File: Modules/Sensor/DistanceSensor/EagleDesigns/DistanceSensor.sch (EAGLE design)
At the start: 10 parts, among them U1 TINY85-20-DIP

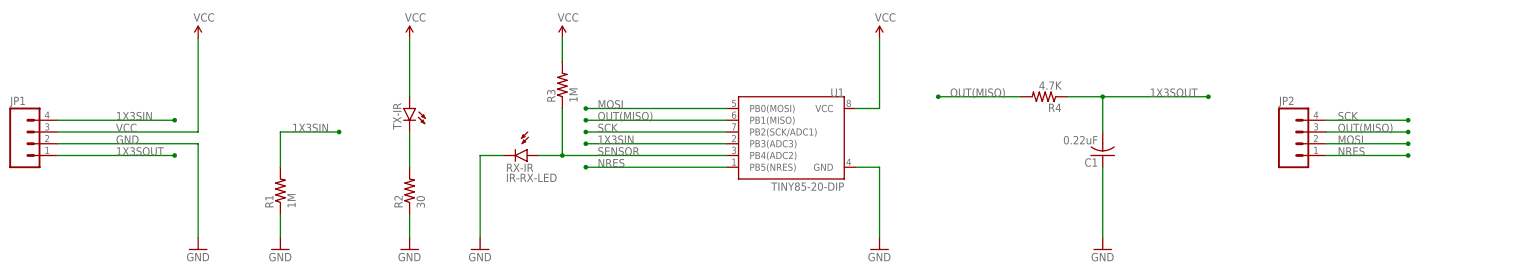
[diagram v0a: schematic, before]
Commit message: DistanceSensor: added another IR-TX LED #9
to increase the range of the module.
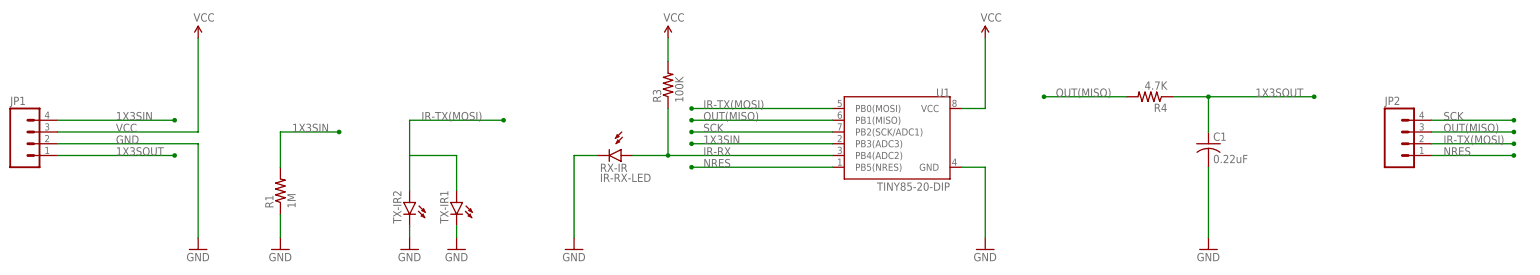
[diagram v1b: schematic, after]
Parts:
- removed R2: 30, adafruit:R-US_R0603
- removed TX-IR: (no value), SparkFun-LED:LED5MM
- added TX-IR1, TX-IR2: (no value), SparkFun-LED:LED5MM
- C1: device adafruit:C-USC0402 -> adafruit:C-USC0603
- R3: value 1M -> 100K
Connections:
- net SENSOR renamed IR-RX
- removed net MOSI: JP2.2, U1.PB0(MOSI)
- removed net N$2: R2.2, TX-IR.C
- new net IR-TX(MOSI): JP2.2, TX-IR1.A, TX-IR2.A, U1.PB0(MOSI)
- net 1X3SOUT: now also C1.1; no longer C1.2
- net GND: now also C1.2, TX-IR1.C, TX-IR2.C; no longer C1.1, R2.1
- net VCC: no longer TX-IR.A
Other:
- moved on the sheet: C1, JP2, R3, R4, RX-IR, U1
